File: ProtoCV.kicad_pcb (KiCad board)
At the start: 2 copper layers, 100 x 100 mm, 142 parts, among them J1 AudioJack2_SwitchT, J10 Conn_01x01_Male, J11 Conn_01x05_Male, J12 Conn_01x09_Male, J13 AudioJack2_SwitchT, J14 AudioJack2_SwitchT, J15 AudioJack2_SwitchT, J16 AudioJack2_SwitchT, J17 AudioJack2_SwitchT, J18 AudioJack2_SwitchT, J19 AudioJack2_SwitchT, J2 AudioJack2_SwitchT, J20 AudioJack2_SwitchT, J21 Conn_01x01_Male, J22 Conn_01x01_Male, J23 Conn_01x01_Male, J24 Conn_01x01_Male, J25 Conn_01x01_Male, J26 Conn_01x01_Male, J27 Conn_01x01_Male, J28 Conn_01x01_Male, J29 Conn_01x01_Male, J3 AudioJack2_SwitchT, J30 Conn_01x01_Male, J4 AudioJack2_SwitchT, J5 AudioJack2_SwitchT, J6 AudioJack2_SwitchT, J7 AudioJack2_SwitchT, J8 AudioJack2_SwitchT, J9 Conn_02x05_Odd_Even, Q1 BC847, Q2 BC847, Q3 BC847, Q4 BC847, Q5 BC847, Q6 BC847, Q7 BC847, Q8 BC847, U1 OPA4192, U2 OPA4192, U3 ADC80508Z, U4 R-78E3.3-0.5, U5 LD2981ABU33TR, U6 74AHCT244, U7 L7805

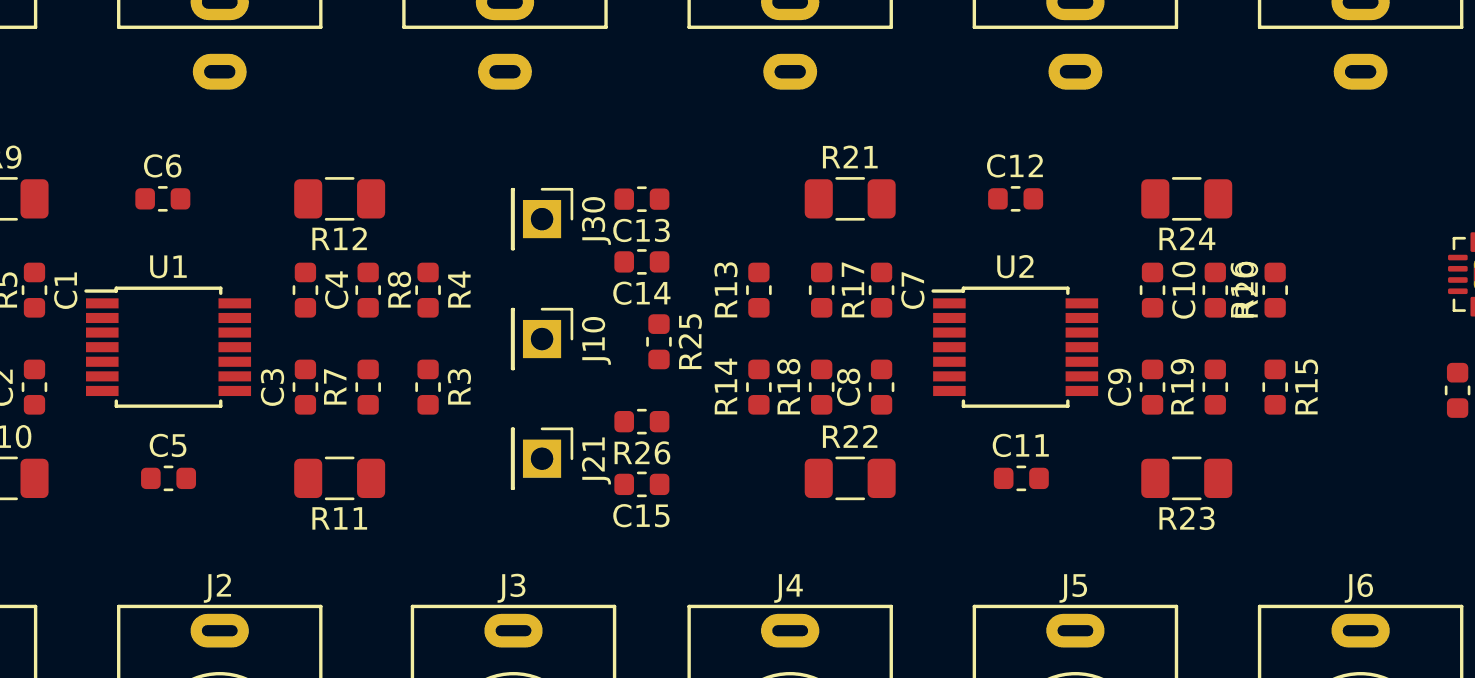
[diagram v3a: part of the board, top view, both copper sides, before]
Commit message: Minor layout adjustments.
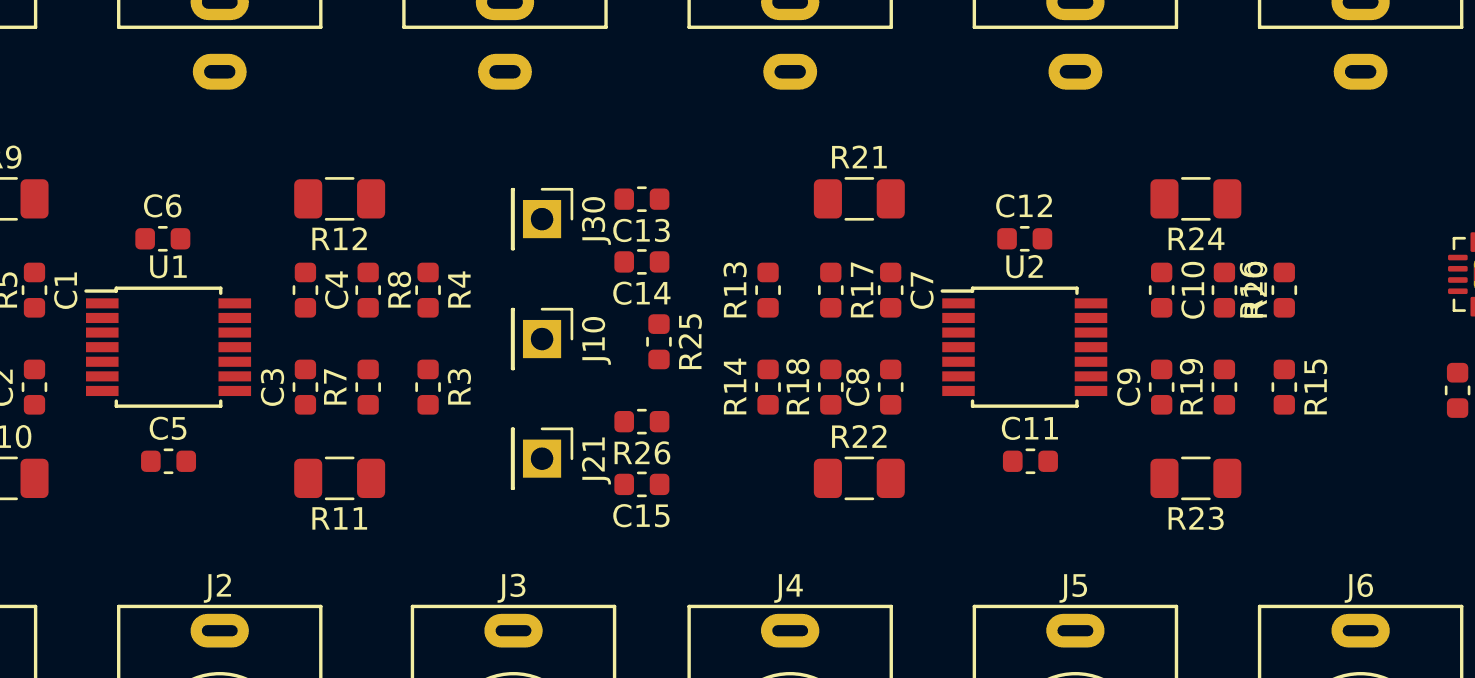
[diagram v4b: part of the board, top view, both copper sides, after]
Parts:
- moved C12 1.82 mm to (154.0, 110.1)
- moved C6 1.78 mm to (115.6, 110.1)
- moved C11 0.86 mm to (154.2, 120.0)
- moved C5 0.76 mm to (115.8, 120.0)
- moved R13 0.41 mm to (142.5, 112.4)
- moved R14 0.41 mm to (142.5, 116.7)
- moved R15 0.41 mm to (165.5, 116.7)
- moved R16 0.41 mm to (165.5, 112.4)
- moved R19 0.41 mm to (162.8, 116.7)
- moved R20 0.41 mm to (162.8, 112.4)
- moved R21 0.41 mm to (146.6, 108.3)
- moved R22 0.41 mm to (146.6, 120.8)
- moved C10 0.41 mm to (160.1, 112.4)
- moved C7 0.41 mm to (148.0, 112.4)
- moved C8 0.41 mm to (148.0, 116.7)
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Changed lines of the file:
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@@
   )
   (module Package_SO:TSSOP-14_4.4x5mm_P0.65mm placed (layer F.Cu)
-    (at 153.548 114.916)
+    (at 153.9544 114.916)
     (descr "14-Lead Plastic Thin Shrink Small Outline (ST)-4.4 mm Body [TSSOP] (see Microchip Packaging Specification 00000049BS.pdf)")
     (tags "SSOP 0.65")
@@
   )
   (module Resistor_SMD:R_1206_3216Metric placed (layer F.Cu)
-    (at 161.168 108.312 180)
+    (at 161.5744 108.312 180)
     (descr "Resistor SMD 1206 (3216 Metric), square (rectangular) end terminal, IPC_7351 nominal, (Body size source: http://www.tortai-tech.com/upload/download/2011102023233369053.pdf), generated with kicad-footprint-generator")
     (tags resistor)
@@
   )
   (module Resistor_SMD:R_1206_3216Metric placed (layer F.Cu)
-    (at 161.168 120.758 180)
+    (at 161.5744 120.758 180)
     (descr "Resistor SMD 1206 (3216 Metric), square (rectangular) end terminal, IPC_7351 nominal, (Body size source: http://www.tortai-tech.com/upload/download/2011102023233369053.pdf), generated with kicad-footprint-generator")
     (tags resistor)
@@
   )
   (module Resistor_SMD:R_1206_3216Metric placed (layer F.Cu)
-    (at 146.182 120.758)
+    (at 146.5884 120.758)
     (descr "Resistor SMD 1206 (3216 Metric), square (rectangular) end terminal, IPC_7351 nominal, (Body size source: http://www.tortai-tech.com/upload/download/2011102023233369053.pdf), generated with kicad-footprint-generator")
     (tags resistor)
@@
   )
   (module Resistor_SMD:R_1206_3216Metric placed (layer F.Cu)
-    (at 146.182 108.312)
+    (at 146.5884 108.312)
     (descr "Resistor SMD 1206 (3216 Metric), square (rectangular) end terminal, IPC_7351 nominal, (Body size source: http://www.tortai-tech.com/upload/download/2011102023233369053.pdf), generated with kicad-footprint-generator")
     (tags resistor)
@@
   )
   (module Resistor_SMD:R_0603_1608Metric placed (layer F.Cu)
-    (at 162.438 112.376 270)
+    (at 162.8444 112.376 270)
     (descr "Resistor SMD 0603 (1608 Metric), square (rectangular) end terminal, IPC_7351 nominal, (Body size source: http://www.tortai-tech.com/upload/download/2011102023233369053.pdf), generated with kicad-footprint-generator")
     (tags resistor)
@@
   )
   (module Resistor_SMD:R_0603_1608Metric placed (layer F.Cu)
-    (at 162.438 116.694 90)
+    (at 162.8444 116.694 90)
     (descr "Resistor SMD 0603 (1608 Metric), square (rectangular) end terminal, IPC_7351 nominal, (Body size source: http://www.tortai-tech.com/upload/download/2011102023233369053.pdf), generated with kicad-footprint-generator")
     (tags resistor)
@@
   )
   (module Resistor_SMD:R_0603_1608Metric placed (layer F.Cu)
-    (at 144.912 116.694 90)
+    (at 145.3184 116.694 90)
     (descr "Resistor SMD 0603 (1608 Metric), square (rectangular) end terminal, IPC_7351 nominal, (Body size source: http://www.tortai-tech.com/upload/download/2011102023233369053.pdf), generated with kicad-footprint-generator")
     (tags resistor)
@@
   )
   (module Resistor_SMD:R_0603_1608Metric placed (layer F.Cu)
-    (at 144.912 112.376 270)
+    (at 145.3184 112.376 270)
     (descr "Resistor SMD 0603 (1608 Metric), square (rectangular) end terminal, IPC_7351 nominal, (Body size source: http://www.tortai-tech.com/upload/download/2011102023233369053.pdf), generated with kicad-footprint-generator")
     (tags resistor)
@@
   )
   (module Resistor_SMD:R_0603_1608Metric placed (layer F.Cu)
-    (at 165.105 112.376 90)
+    (at 165.5114 112.376 90)
     (descr "Resistor SMD 0603 (1608 Metric), square (rectangular) end terminal, IPC_7351 nominal, (Body size source: http://www.tortai-tech.com/upload/download/2011102023233369053.pdf), generated with kicad-footprint-generator")
     (tags resistor)
@@
   )
   (module Resistor_SMD:R_0603_1608Metric placed (layer F.Cu)
-    (at 165.105 116.694 270)
+    (at 165.5114 116.694 270)
     (descr "Resistor SMD 0603 (1608 Metric), square (rectangular) end terminal, IPC_7351 nominal, (Body size source: http://www.tortai-tech.com/upload/download/2011102023233369053.pdf), generated with kicad-footprint-generator")
     (tags resistor)
@@
   )
   (module Resistor_SMD:R_0603_1608Metric placed (layer F.Cu)
-    (at 142.118 116.694 90)
+    (at 142.5244 116.694 90)
     (descr "Resistor SMD 0603 (1608 Metric), square (rectangular) end terminal, IPC_7351 nominal, (Body size source: http://www.tortai-tech.com/upload/download/2011102023233369053.pdf), generated with kicad-footprint-generator")
     (tags resistor)
@@
   )
   (module Resistor_SMD:R_0603_1608Metric placed (layer F.Cu)
-    (at 142.118 112.376 90)
+    (at 142.5244 112.376 90)
     (descr "Resistor SMD 0603 (1608 Metric), square (rectangular) end terminal, IPC_7351 nominal, (Body size source: http://www.tortai-tech.com/upload/download/2011102023233369053.pdf), generated with kicad-footprint-generator")
     (tags resistor)
@@
   )
   (module Capacitor_SMD:C_0603_1608Metric placed (layer F.Cu)
-    (at 153.548 108.312)
+    (at 153.9544 110.09)
     (descr "Capacitor SMD 0603 (1608 Metric), square (rectangular) end terminal, IPC_7351 nominal, (Body size source: http://www.tortai-tech.com/upload/download/2011102023233369053.pdf), generated with kicad-footprint-generator")
     (tags capacitor)
@@
   )
   (module Capacitor_SMD:C_0603_1608Metric placed (layer F.Cu)
-    (at 153.802 120.758)
+    (at 154.2084 119.996)
     (descr "Capacitor SMD 0603 (1608 Metric), square (rectangular) end terminal, IPC_7351 nominal, (Body size source: http://www.tortai-tech.com/upload/download/2011102023233369053.pdf), generated with kicad-footprint-generator")
     (tags capacitor)
@@
   )
   (module Capacitor_SMD:C_0603_1608Metric placed (layer F.Cu)
-    (at 159.644 112.376 270)
+    (at 160.0504 112.376 270)
     (descr "Capacitor SMD 0603 (1608 Metric), square (rectangular) end terminal, IPC_7351 nominal, (Body size source: http://www.tortai-tech.com/upload/download/2011102023233369053.pdf), generated with kicad-footprint-generator")
     (tags capacitor)
@@
   )
   (module Capacitor_SMD:C_0603_1608Metric placed (layer F.Cu)
-    (at 159.644 116.694 90)
+    (at 160.0504 116.694 90)
     (descr "Capacitor SMD 0603 (1608 Metric), square (rectangular) end terminal, IPC_7351 nominal, (Body size source: http://www.tortai-tech.com/upload/download/2011102023233369053.pdf), generated with kicad-footprint-generator")
     (tags capacitor)
@@
   )
   (module Capacitor_SMD:C_0603_1608Metric placed (layer F.Cu)
-    (at 147.579 116.694 90)
+    (at 147.9854 116.694 90)
     (descr "Capacitor SMD 0603 (1608 Metric), square (rectangular) end terminal, IPC_7351 nominal, (Body size source: http://www.tortai-tech.com/upload/download/2011102023233369053.pdf), generated with kicad-footprint-generator")
     (tags capacitor)
@@
   )
   (module Capacitor_SMD:C_0603_1608Metric placed (layer F.Cu)
-    (at 147.579 112.376 270)
+    (at 147.9854 112.376 270)
     (descr "Capacitor SMD 0603 (1608 Metric), square (rectangular) end terminal, IPC_7351 nominal, (Body size source: http://www.tortai-tech.com/upload/download/2011102023233369053.pdf), generated with kicad-footprint-generator")
     (tags capacitor)
@@
   )
   (module Capacitor_SMD:C_0603_1608Metric placed (layer F.Cu)
-    (at 115.575 108.312)
+    (at 115.575 110.09)
     (descr "Capacitor SMD 0603 (1608 Metric), square (rectangular) end terminal, IPC_7351 nominal, (Body size source: http://www.tortai-tech.com/upload/download/2011102023233369053.pdf), generated with kicad-footprint-generator")
     (tags capacitor)
@@
   )
   (module Capacitor_SMD:C_0603_1608Metric placed (layer F.Cu)
-    (at 115.829 120.758)
+    (at 115.829 119.996)
     (descr "Capacitor SMD 0603 (1608 Metric), square (rectangular) end terminal, IPC_7351 nominal, (Body size source: http://www.tortai-tech.com/upload/download/2011102023233369053.pdf), generated with kicad-footprint-generator")
     (tags capacitor)

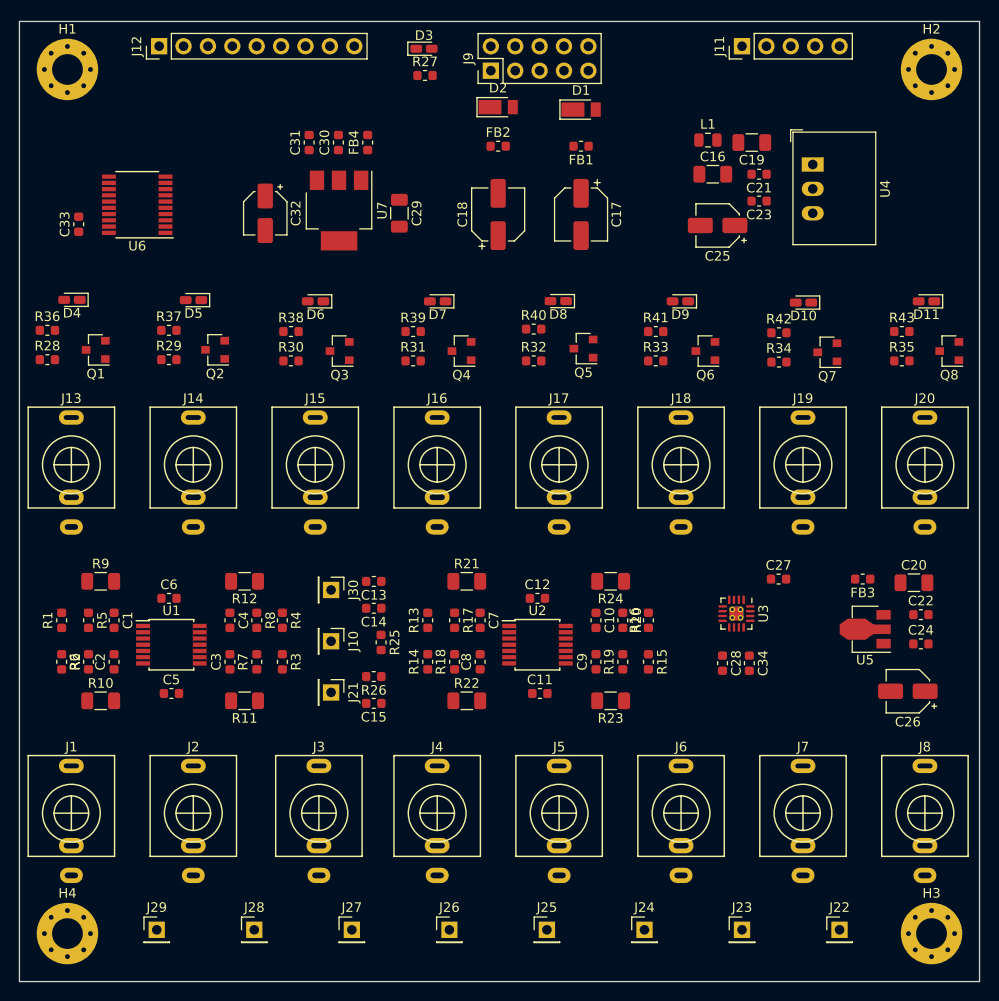
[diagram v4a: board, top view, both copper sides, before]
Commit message: Power routing and split ground pour.
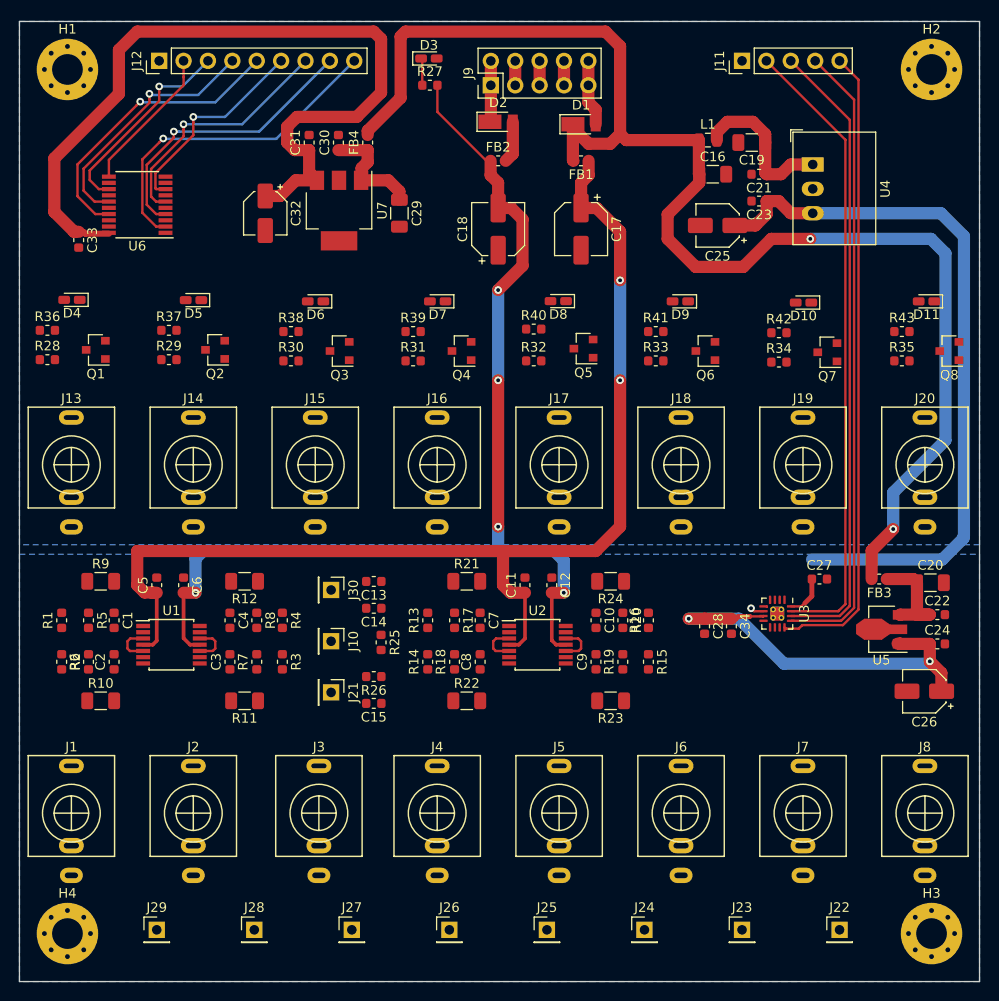
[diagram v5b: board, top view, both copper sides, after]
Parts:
- moved C11 11.4 mm to (152.7, 108.7), turned to 90 degrees
- moved C5 11.4 mm to (114.3, 108.7), turned to 90 degrees
- moved C28 4.28 mm to (171.4, 113.0)
- moved C34 4.28 mm to (174.2, 113.0)
- moved C27 4.25 mm to (183.3, 108.1)
- moved U3 4.25 mm to (178.9, 111.7)
- moved C6 2.05 mm to (117.1, 108.7), turned to 270 degrees
- moved C12 2.03 mm to (155.4, 108.7), turned to 270 degrees
- moved C22 1.71 mm to (195.6, 111.8)
- moved C24 1.71 mm to (195.6, 114.8)
- moved FB3 1.71 mm to (189.5, 108.1)
- moved C20 1.71 mm to (194.9, 108.5)
- moved C26 1.71 mm to (194.2, 119.8)
- moved U5 1.71 mm to (190.2, 113.3)
- moved C33 1.65 mm to (106.2, 72.8), turned to 270 degrees
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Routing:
- net Net-(C16-Pad1): track 0.00 -> 144.0 mm, vias 0 -> 2
- net +12V: track 0.00 -> 117.8 mm, vias 0 -> 2
- net -12V: track 0.00 -> 116.1 mm, vias 0 -> 5
- net +5V: track 0.00 -> 85.4 mm
- net +3V3: track 0.00 -> 79.7 mm
- net Net-(J11-Pad5): track 0.00 -> 66.5 mm
- net Net-(J11-Pad2): track 0.00 -> 66.0 mm
- net Net-(J11-Pad3): track 0.00 -> 65.9 mm
- net Net-(J11-Pad4): track 0.00 -> 65.8 mm
- net +3.3VA: track 0.00 -> 43.9 mm, vias 0 -> 2
- net Net-(J12-Pad9): track 0.00 -> 34.9 mm, vias 0 -> 1
- net Net-(J12-Pad5): track 0.00 -> 30.6 mm, vias 0 -> 1
- net Net-(J12-Pad8): track 0.00 -> 30.5 mm, vias 0 -> 1
- net Net-(J12-Pad4): track 0.00 -> 26.2 mm, vias 0 -> 1
- net Net-(J12-Pad7): track 0.00 -> 26.1 mm, vias 0 -> 1
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- added copper zone on B.Cu, net GND

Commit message: Lots of manual routing.
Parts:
- turned Q1 to 270 degrees
- turned Q2 to 270 degrees
- turned Q3 to 270 degrees
- turned Q4 to 270 degrees
- turned Q5 to 270 degrees
- turned Q6 to 270 degrees
- turned Q7 to 270 degrees
- turned Q8 to 270 degrees
- turned R14 to 270 degrees
- turned R36 to 180 degrees
- turned R37 to 180 degrees
- turned R38 to 180 degrees
- turned R39 to 180 degrees
- turned R4 to 90 degrees
- turned R40 to 180 degrees
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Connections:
- R10 pad 1: CV1 -> CV7
- R11 pad 1: CV2 -> CV6
- R12 pad 1: CV3 -> CV1
- R13 pad 2: OUT4 -> OUT2
- R15 pad 2: OUT6 -> OUT4
- R16 pad 2: OUT7 -> OUT3
- R17 pad 1: CV4 -> CV2
- R19 pad 1: CV6 -> CV4
- R2 pad 2: OUT1 -> OUT7
- R20 pad 1: CV7 -> CV3
- R21 pad 1: CV4 -> CV2
- R23 pad 1: CV6 -> CV4
- R24 pad 1: CV7 -> CV3
- R3 pad 2: OUT2 -> OUT6
- R4 pad 2: OUT3 -> OUT1
- R6 pad 1: CV1 -> CV7
- R7 pad 1: CV2 -> CV6
- R8 pad 1: CV3 -> CV1
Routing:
- net +12V: track 117.8 -> 301.8 mm, vias 2 -> 4
- net OUT7: track 0.00 -> 83.6 mm
- net OUT0: track 0.00 -> 79.8 mm, vias 0 -> 2
- net OUT6: track 0.00 -> 58.5 mm
- net VREF: track 0.00 -> 57.2 mm, vias 0 -> 2
- net OUT1: track 0.00 -> 54.2 mm, vias 0 -> 2
- net BIAS: track 16.9 -> 70.6 mm
- net TRIG3: track 0.00 -> 53.6 mm, vias 0 -> 2
- net OUT5: track 0.00 -> 43.5 mm
- net TRIG2: track 0.00 -> 41.7 mm
- net OUT2: track 0.00 -> 41.2 mm, vias 0 -> 2
- net TRIG1: track 0.00 -> 25.5 mm
- net TRIG0: track 0.00 -> 20.9 mm
- net OUT4: track 0.00 -> 15.6 mm
- net OUT3: track 0.05 -> 12.9 mm
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
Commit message: Front side pours.
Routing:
- added copper zone on F.Cu, net GND
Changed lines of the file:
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@@
+    )
+  )
+  (zone (net 108) (net_name GND) (layer F.Cu) (hatch edge 0.508)
+    (connect_pads (clearance 0.508))
+    (min_thickness 0.254)
+    (fill yes (arc_segments 32) (thermal_gap 0.508) (thermal_bridge_width 0.508))
+    (polygon
+      (pts
+        (xy 200 104.5) (xy 100 104.5) (xy 100 50) (xy 200 50)
+      )
+    )
+  )
+  (zone (net 108) (net_name GND) (layer F.Cu) (hatch edge 0.508)
+    (connect_pads (clearance 0.508))
+    (min_thickness 0.254)
+    (fill yes (arc_segments 32) (thermal_gap 0.508) (thermal_bridge_width 0.508))
+    (polygon
+      (pts
+        (xy 200 150) (xy 100 150) (xy 100 105.5) (xy 200 105.5)
+      )
     )
   )

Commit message: Near complete manual routing.
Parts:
- moved J3 0.38 mm to (130.8, 132.5)
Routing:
- net CV7: track 3.33 -> 122.5 mm
- net CV6: track 3.33 -> 98.1 mm, vias 0 -> 2
- net TRIG7: track 6.63 -> 94.6 mm, vias 0 -> 2
- net CV3: track 3.33 -> 75.4 mm, vias 0 -> 1
- net TRIG6: track 6.74 -> 78.4 mm
- net TRIG5: track 6.86 -> 65.1 mm
- net CV1: track 3.33 -> 52.7 mm, vias 0 -> 2
- net CV5: track 3.33 -> 51.4 mm, vias 0 -> 2
- net CV2: track 3.33 -> 50.3 mm, vias 0 -> 2
- net TRIG4: track 6.98 -> 51.9 mm
- net CV0: track 3.33 -> 44.7 mm
- net CV4: track 3.33 -> 35.5 mm, vias 0 -> 1
- net OUT7: track 83.6 -> 86.0 mm
- net BIAS: track 70.6 -> 68.7 mm
- net Net-(J12-Pad6): track 21.7 -> 22.8 mm
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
